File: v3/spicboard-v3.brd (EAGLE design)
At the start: 65 x 60 mm, 40 parts, among them IC1 74HC595, Q1 BC557, Q2 BC557

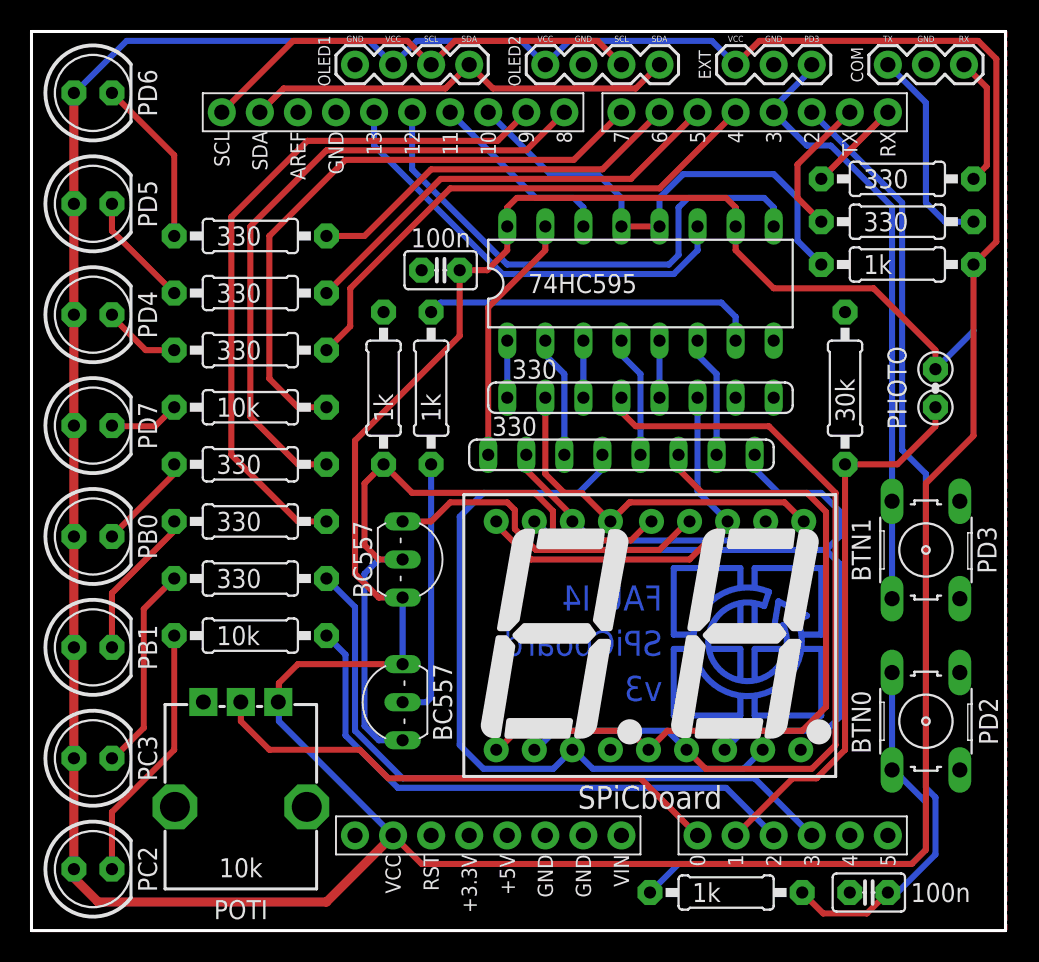
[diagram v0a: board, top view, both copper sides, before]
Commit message: SPiCboard v3: Photowiderstand durch Phototransistor ersetzt
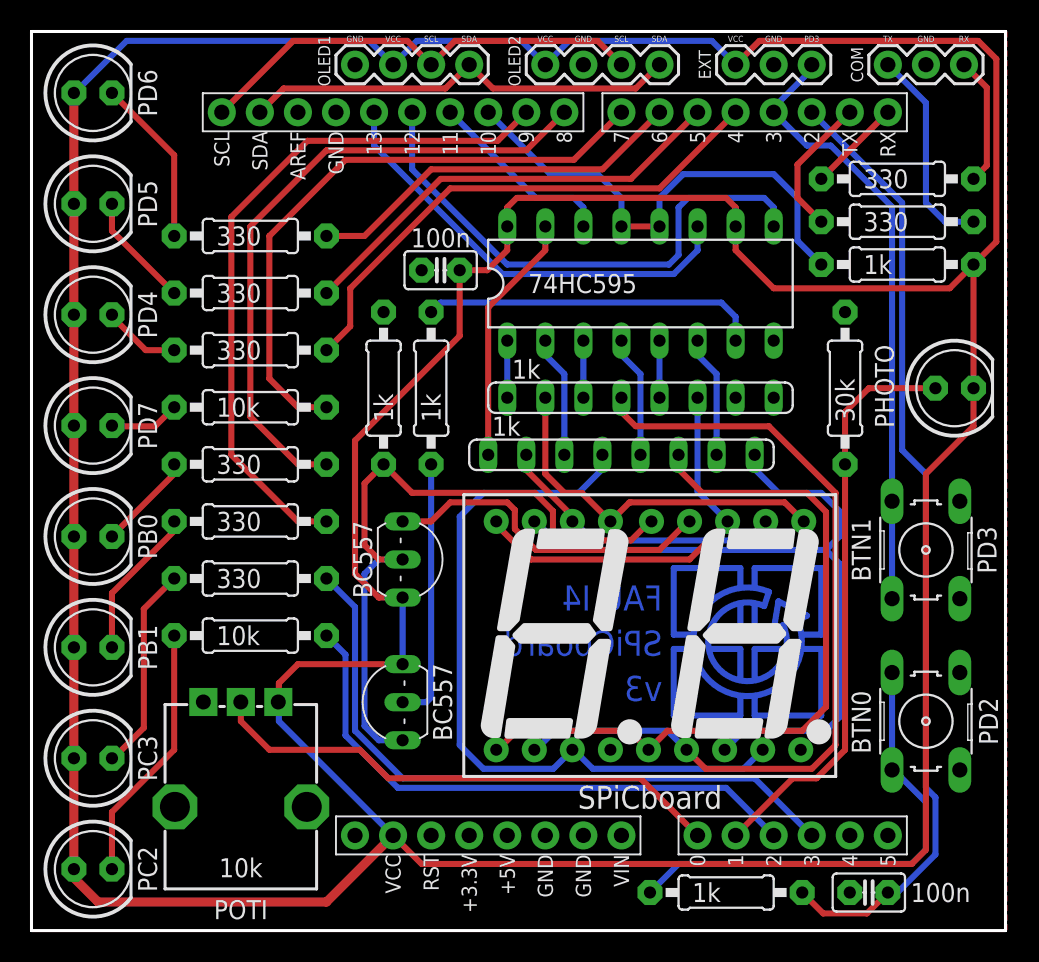
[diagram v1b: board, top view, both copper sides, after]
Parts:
- PHOTO: value LDR -> PTPT5MM; device spicboard-v3:LDR -> spicboard-v3:PT5MM
- RN1, RN2: value 330 -> 1k
- moved PHOTO 1.27 mm to (61.6, 36.2), turned to 0 degrees
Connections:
- net LDR: now also PHOTO.E; no longer PHOTO.1
- net VCC: now also PHOTO.C; no longer PHOTO.2
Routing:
- net VCC: track 339.4 -> 331.6 mm
- net LDR: track 37.1 -> 38.9 mm

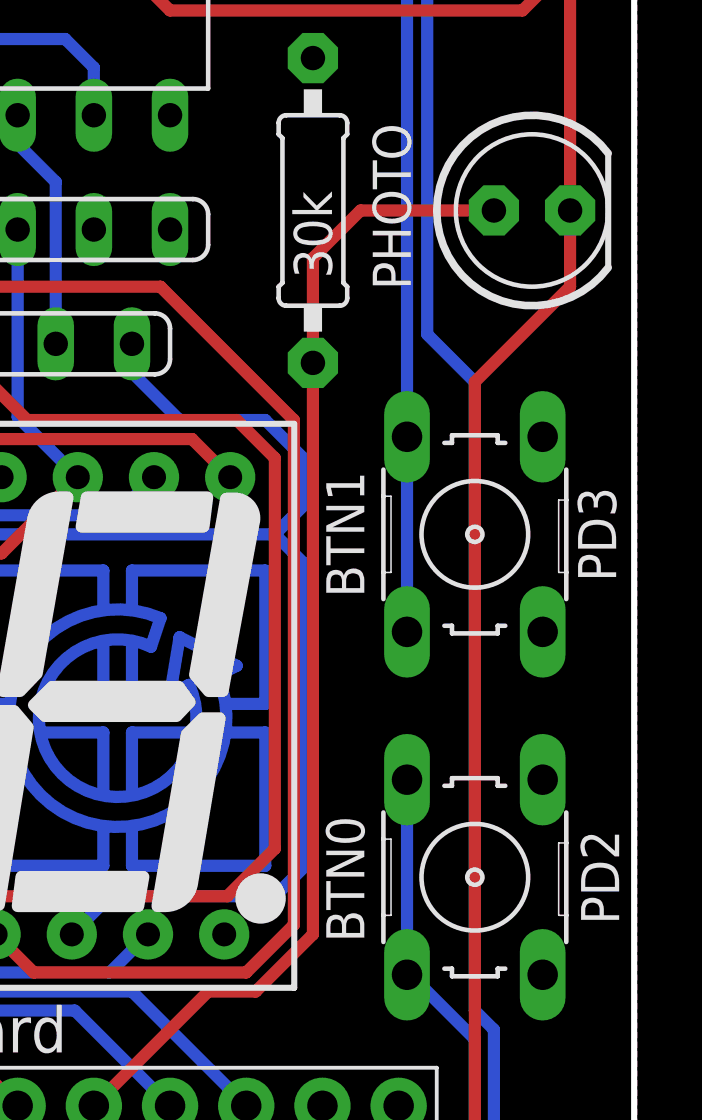
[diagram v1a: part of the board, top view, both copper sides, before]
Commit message: Phototransistor 5mm
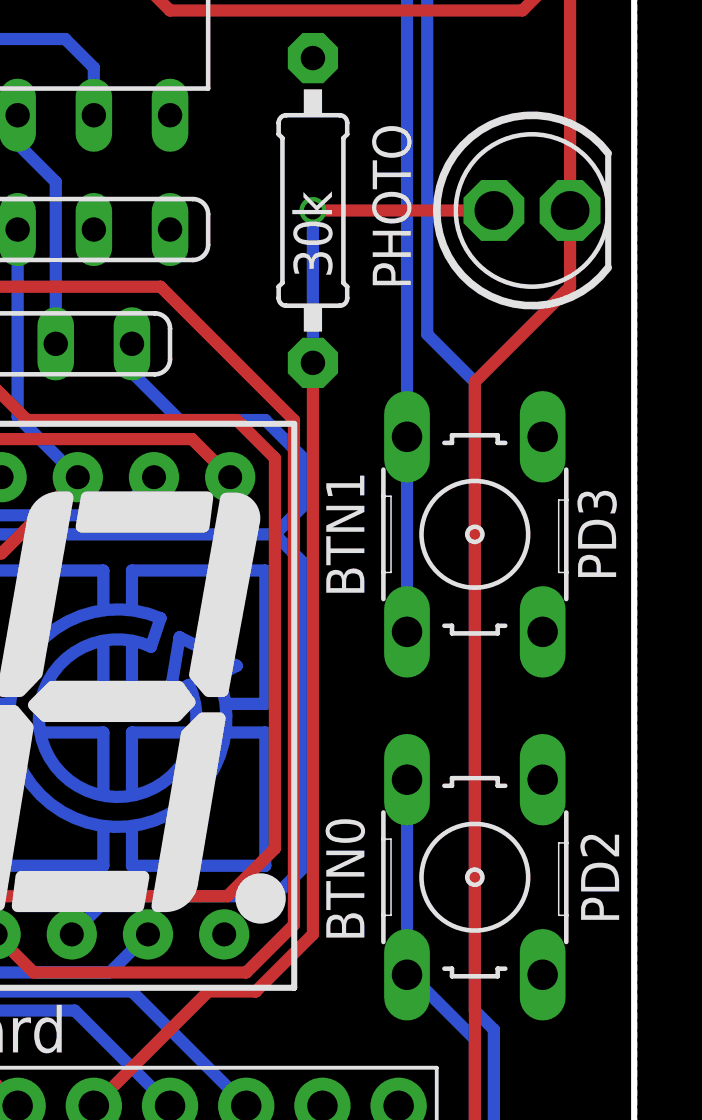
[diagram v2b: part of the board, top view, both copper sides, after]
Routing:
- net LDR: track 38.9 -> 39.8 mm, vias 0 -> 1
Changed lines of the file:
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@@
 <contactref element="B1" pad="A1"/>
 <wire x1="52.3875" y1="10.16" x2="54.2925" y2="12.065" width="0.4064" layer="1"/>
-<wire x1="54.2925" y1="31.115" x2="54.2925" y2="12.065" width="0.4064" layer="1"/>
+<wire x1="54.2925" y1="12.065" x2="54.2925" y2="31.115" width="0.4064" layer="1"/>
 <wire x1="52.3875" y1="10.16" x2="50.8" y2="10.16" width="0.4064" layer="1"/>
 <wire x1="50.8" y1="10.16" x2="46.99" y2="6.35" width="0.4064" layer="1"/>
 <contactref element="PHOTO" pad="E"/>
-<wire x1="60.325" y1="36.195" x2="55.88" y2="36.195" width="0.4064" layer="1"/>
-<wire x1="55.88" y1="36.195" x2="54.2925" y2="34.6075" width="0.4064" layer="1"/>
-<wire x1="54.2925" y1="34.6075" x2="54.2925" y2="31.115" width="0.4064" layer="1"/>
+<via x="54.2925" y="36.195" extent="1-16" drill="0.6"/>
+<wire x1="54.2925" y1="36.195" x2="54.2925" y2="31.115" width="0.4064" layer="16"/>
+<wire x1="60.325" y1="36.195" x2="54.2925" y2="36.195" width="0.4064" layer="1"/>
 </signal>
 <signal name="L0">

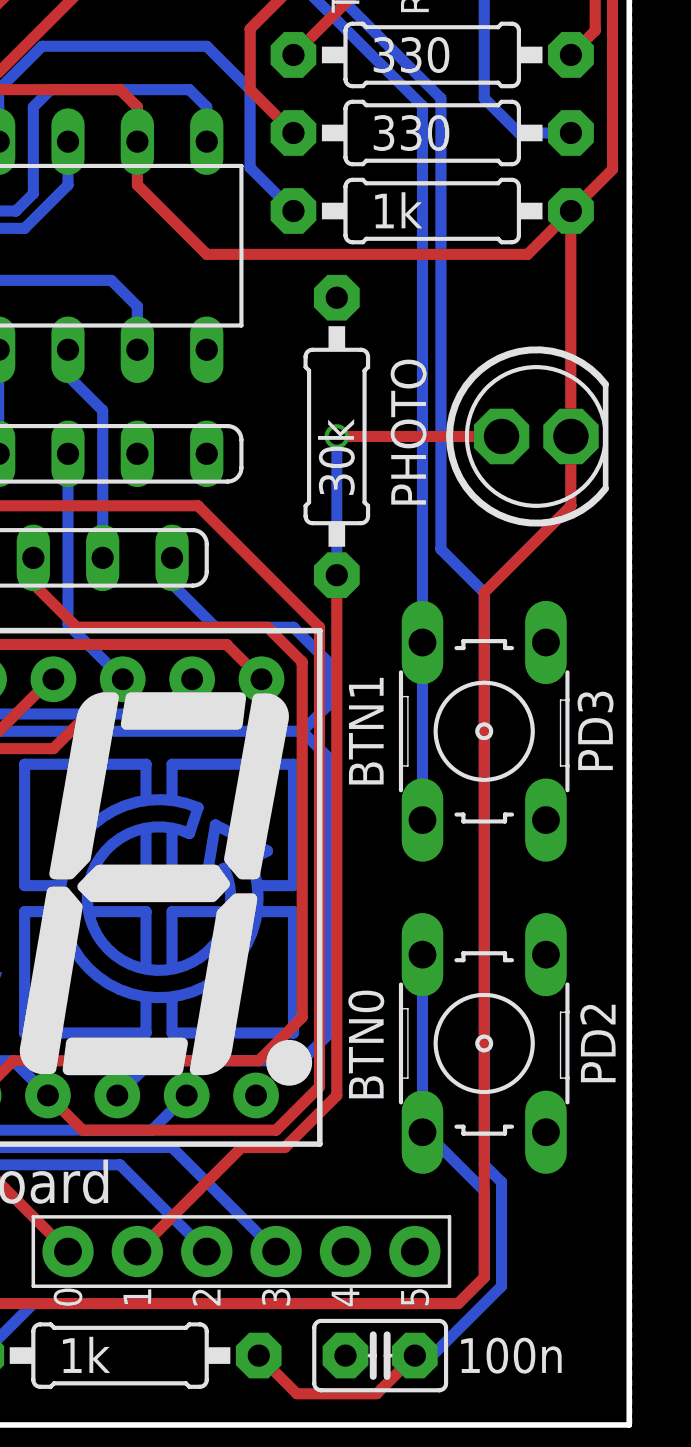
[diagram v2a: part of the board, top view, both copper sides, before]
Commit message: SPiCboard: Kleiner Phototransistor, 7-Seg 1k Ohm
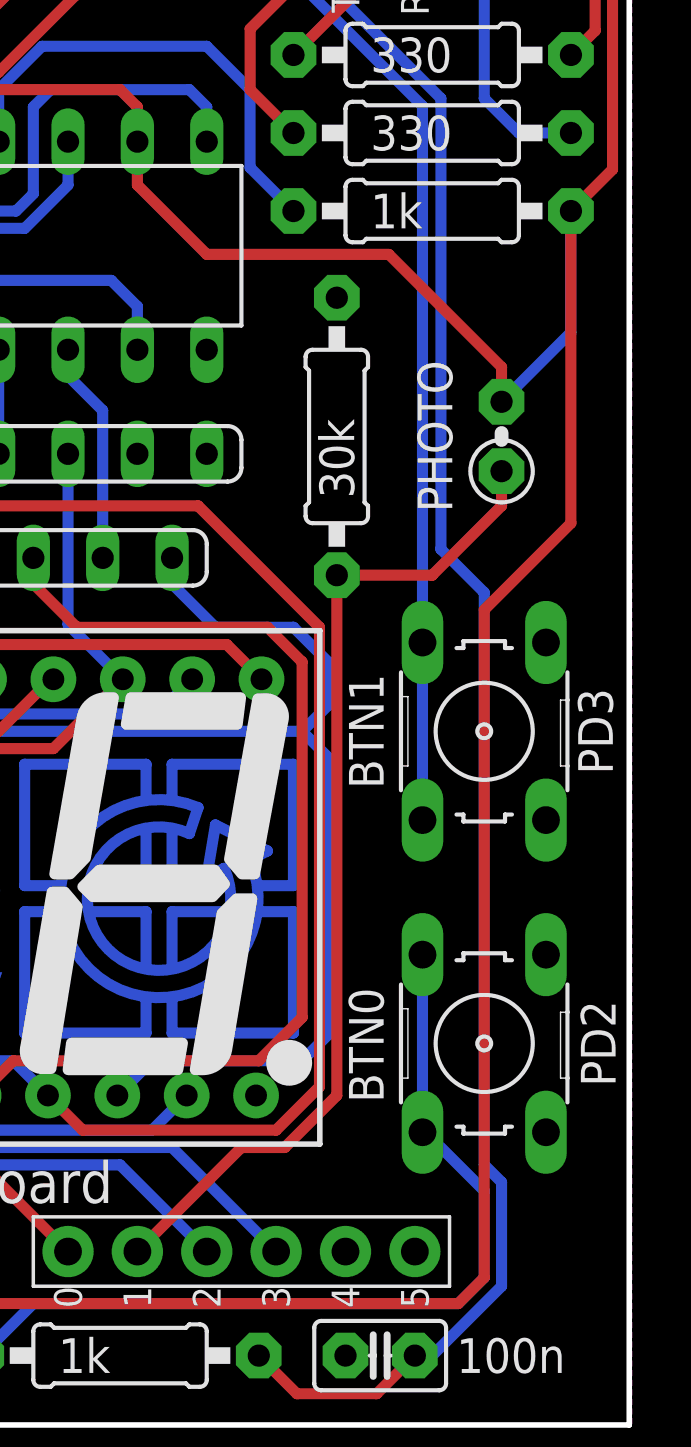
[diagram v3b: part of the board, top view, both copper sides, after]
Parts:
- PHOTO: value PTPT5MM -> PTPT; device spicboard-v3:PT5MM -> spicboard-v3:PT
- moved PHOTO 1.27 mm to (60.3, 36.2), turned to 90 degrees
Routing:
- net VCC: track 331.6 -> 339.4 mm
- net LDR: track 39.8 -> 37.1 mm, vias 1 -> 0
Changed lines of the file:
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@@
 <attribute name="VALUE" x="45.72" y="55.753" size="0.6096" layer="27" font="vector" ratio="20"/>
 </element>
-<element name="PHOTO" library="spicboard-v3" package="PT5MM" value="PTPT5MM" x="61.595" y="36.195" smashed="yes">
-<attribute name="NAME" x="57.5564" y="36.322" size="1.27" layer="25" ratio="10" rot="R270" align="top-center"/>
-</element>
+<element name="PHOTO" library="spicboard-v3" package="PT" value="PTPT" x="60.325" y="36.195" rot="R90"/>
 </elements>
 <signals>
@@
 <wire x1="35.8775" y1="59.3725" x2="45.4025" y2="59.3725" width="0.4064" layer="16"/>
 <wire x1="58.7375" y1="4.445" x2="59.69" y2="5.3975" width="0.4064" layer="1"/>
-<wire x1="59.69" y1="5.3975" x2="59.69" y2="30.48" width="0.4064" layer="1"/>
+<wire x1="59.69" y1="5.3975" x2="59.69" y2="29.845" width="0.4064" layer="1"/>
 <wire x1="63.1825" y1="59.3725" x2="64.389" y2="58.166" width="0.4064" layer="1"/>
 <wire x1="63.1825" y1="59.3725" x2="48.5775" y2="59.3725" width="0.4064" layer="1"/>
@@
 <wire x1="46.99" y1="48.26" x2="46.99" y2="46.99" width="0.4064" layer="1"/>
 <wire x1="46.99" y1="45.4025" x2="49.53" y2="42.8625" width="0.4064" layer="1"/>
-<wire x1="62.865" y1="33.655" x2="59.69" y2="30.48" width="0.4064" layer="1"/>
+<wire x1="62.865" y1="33.02" x2="59.69" y2="29.845" width="0.4064" layer="1"/>
 <contactref element="R15" pad="2"/>
-<wire x1="62.865" y1="44.45" x2="64.389" y2="45.974" width="0.4064" layer="1"/>
+<wire x1="64.389" y1="45.974" x2="62.865" y2="44.45" width="0.4064" layer="1"/>
 <wire x1="64.389" y1="58.166" x2="64.389" y2="45.974" width="0.4064" layer="1"/>
+<wire x1="62.865" y1="44.45" x2="62.865" y2="33.02" width="0.4064" layer="1"/>
+<wire x1="62.865" y1="44.45" x2="62.865" y2="40.005" width="0.4064" layer="16"/>
 <contactref element="EXT" pad="1"/>
 <wire x1="48.5775" y1="59.3725" x2="46.99" y2="57.785" width="0.4064" layer="1"/>
 <wire x1="45.4025" y1="59.3725" x2="46.99" y2="57.785" width="0.4064" layer="16"/>
+<wire x1="56.1975" y1="42.8625" x2="60.325" y2="38.735" width="0.4064" layer="1"/>
+<wire x1="49.53" y1="42.8625" x2="56.1975" y2="42.8625" width="0.4064" layer="1"/>
 <contactref element="PHOTO" pad="C"/>
-<wire x1="62.865" y1="44.45" x2="62.865" y2="36.195" width="0.4064" layer="1"/>
-<wire x1="62.865" y1="36.195" x2="62.865" y2="33.655" width="0.4064" layer="1"/>
-<wire x1="61.2775" y1="42.8625" x2="62.865" y2="44.45" width="0.4064" layer="1"/>
-<wire x1="49.53" y1="42.8625" x2="61.2775" y2="42.8625" width="0.4064" layer="1"/>
+<wire x1="60.325" y1="38.735" x2="60.325" y2="37.465" width="0.4064" layer="1"/>
+<wire x1="62.865" y1="40.005" x2="60.325" y2="37.465" width="0.4064" layer="16"/>
 </signal>
 <signal name="N$2">
@@
 <wire x1="52.3875" y1="10.16" x2="50.8" y2="10.16" width="0.4064" layer="1"/>
 <wire x1="50.8" y1="10.16" x2="46.99" y2="6.35" width="0.4064" layer="1"/>
+<wire x1="57.785" y1="31.115" x2="60.325" y2="33.655" width="0.4064" layer="1"/>
+<wire x1="54.2925" y1="31.115" x2="57.785" y2="31.115" width="0.4064" layer="1"/>
 <contactref element="PHOTO" pad="E"/>
-<via x="54.2925" y="36.195" extent="1-16" drill="0.6"/>
-<wire x1="54.2925" y1="36.195" x2="54.2925" y2="31.115" width="0.4064" layer="16"/>
-<wire x1="60.325" y1="36.195" x2="54.2925" y2="36.195" width="0.4064" layer="1"/>
+<wire x1="60.325" y1="33.655" x2="60.325" y2="34.925" width="0.4064" layer="1"/>
 </signal>
 <signal name="L0">

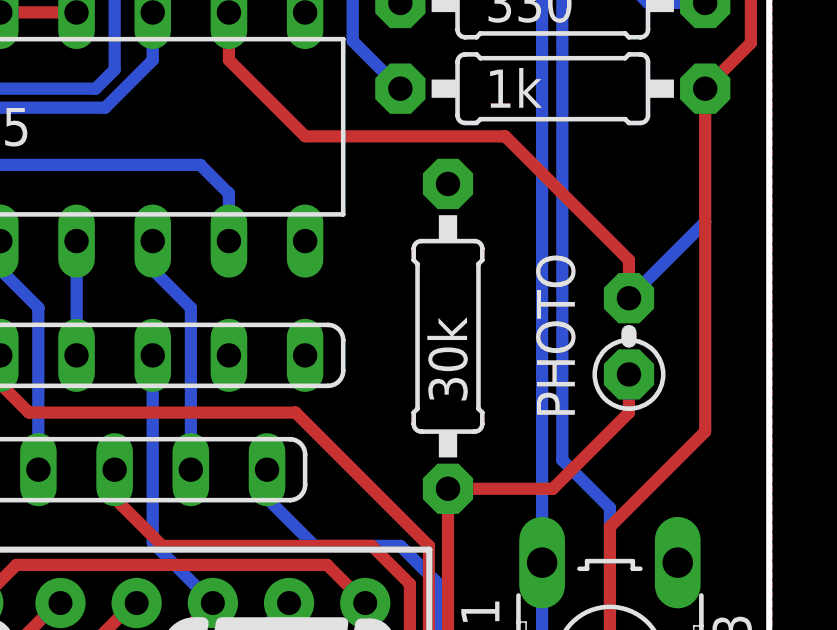
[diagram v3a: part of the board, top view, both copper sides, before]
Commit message: Phototransistor 49.9k
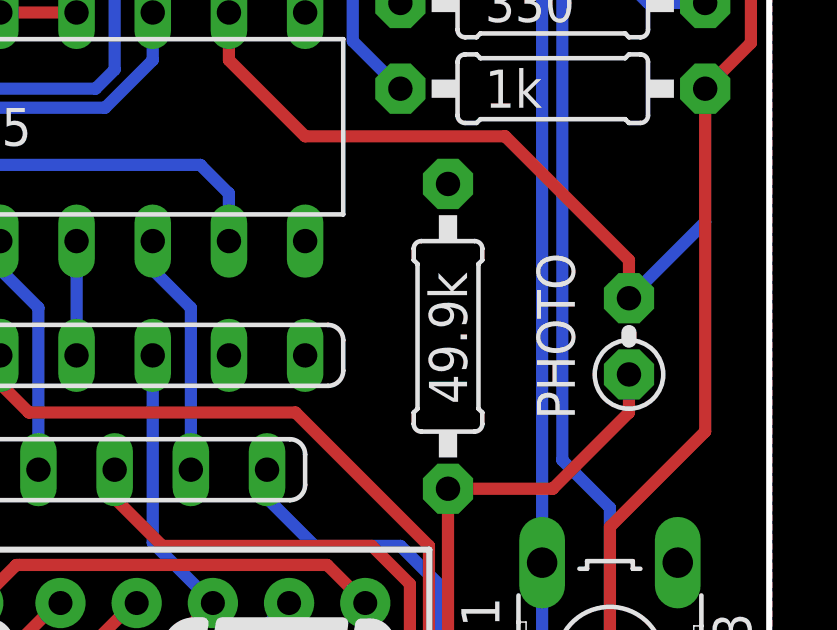
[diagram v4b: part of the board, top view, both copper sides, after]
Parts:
- R10: value 30k -> 49.9k
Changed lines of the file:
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@@
 <attribute name="OC_NEWARK" value="unknown" x="41.275" y="19.685" size="1.778" layer="25" display="off"/>
 </element>
-<element name="R10" library="spicboard-v3" package="0207/10" value="30k" x="54.2925" y="36.195" smashed="yes" rot="R270">
+<element name="R10" library="spicboard-v3" package="0207/10" value="49.9k" x="54.2925" y="36.195" smashed="yes" rot="R270">
 <attribute name="VALUE" x="54.9275" y="33.9344" size="1.27" layer="25" ratio="10" rot="R90"/>
 </element>

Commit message: Phototransistor 100k
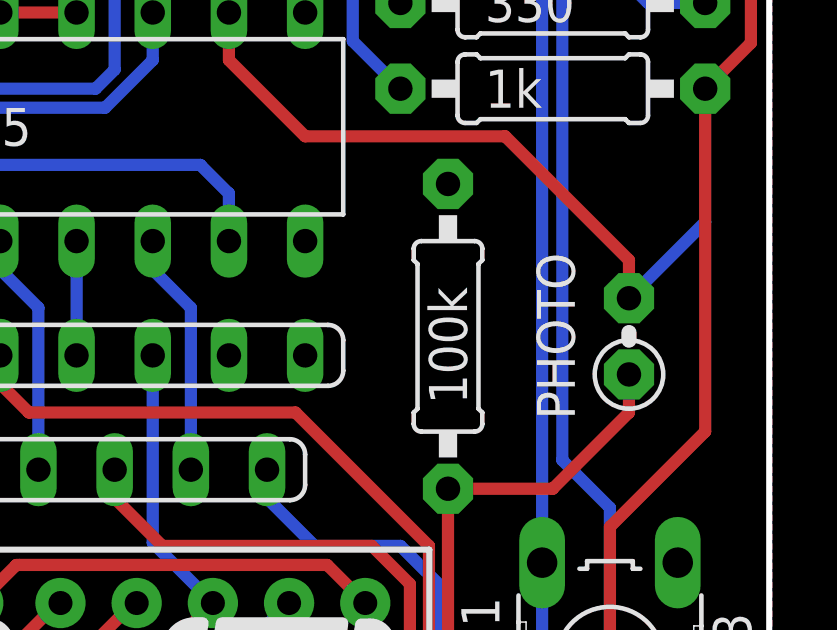
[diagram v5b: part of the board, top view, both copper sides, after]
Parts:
- R10: value 49.9k -> 100k
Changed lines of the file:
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@@
 <attribute name="OC_NEWARK" value="unknown" x="41.275" y="19.685" size="1.778" layer="25" display="off"/>
 </element>
-<element name="R10" library="spicboard-v3" package="0207/10" value="49.9k" x="54.2925" y="36.195" smashed="yes" rot="R270">
+<element name="R10" library="spicboard-v3" package="0207/10" value="100k" x="54.2925" y="36.195" smashed="yes" rot="R270">
 <attribute name="VALUE" x="54.9275" y="33.9344" size="1.27" layer="25" ratio="10" rot="R90"/>
 </element>

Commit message: Photowiderstand
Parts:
- R10: value 100k -> R
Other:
- board text added: "PHOTO"
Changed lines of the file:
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@@
 <vertex x="29.21" y="24.9555"/>
 </polygon>
+<text x="54.9275" y="35.2425" size="0.635" layer="25" rot="R90">PHOTO</text>
 </plain>
 <attributes>
@@
 <attribute name="OC_NEWARK" value="unknown" x="41.275" y="19.685" size="1.778" layer="25" display="off"/>
 </element>
-<element name="R10" library="spicboard-v3" package="0207/10" value="100k" x="54.2925" y="36.195" smashed="yes" rot="R270">
+<element name="R10" library="spicboard-v3" package="0207/10" value="R" x="54.2925" y="36.195" smashed="yes" rot="R270">
 <attribute name="VALUE" x="54.9275" y="33.9344" size="1.27" layer="25" ratio="10" rot="R90"/>
 </element>
